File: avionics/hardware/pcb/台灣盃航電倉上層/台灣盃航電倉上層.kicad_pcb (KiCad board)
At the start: 4 copper layers, 80 x 80 mm, 38 parts, among them J1 SMA, J2 SMA, U1 LIS3MDL, U2 NEO-M9N, U3 E22-900T22S, U4 Connector

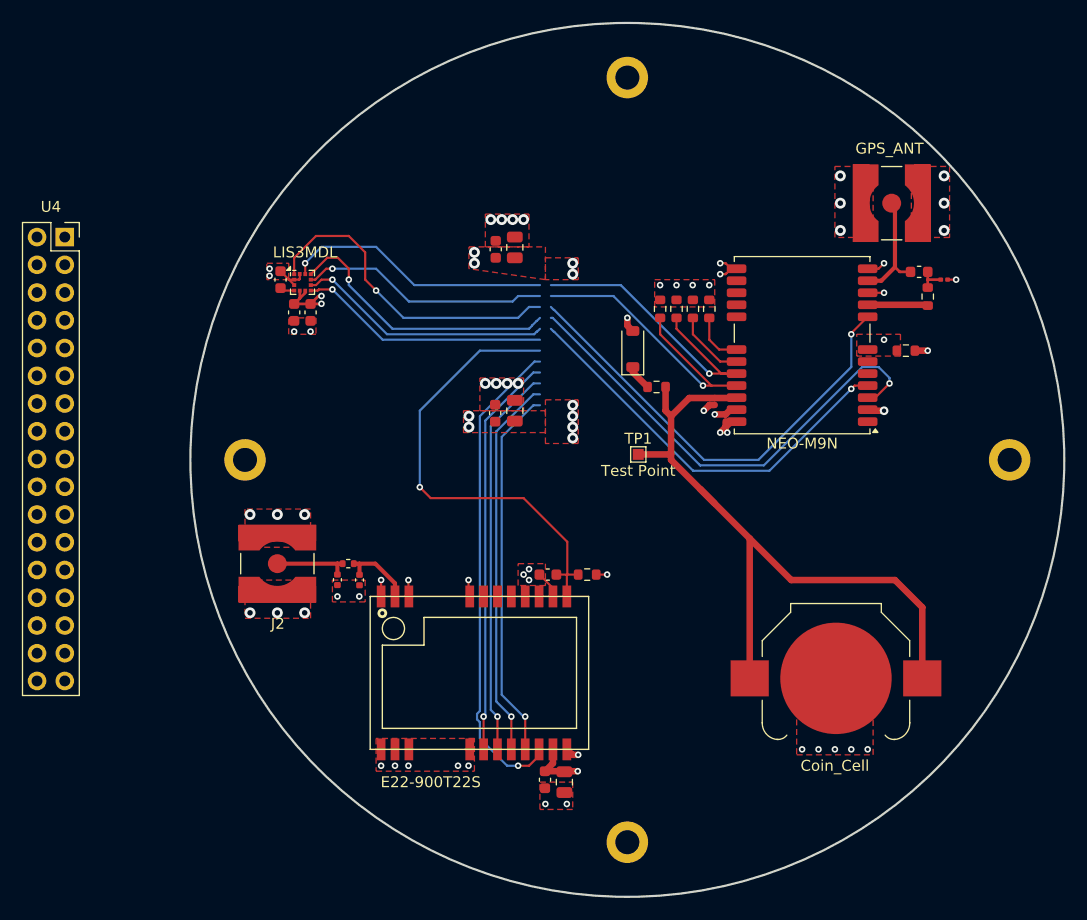
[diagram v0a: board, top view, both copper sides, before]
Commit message: 對上層PCB的布局進行了一些修改
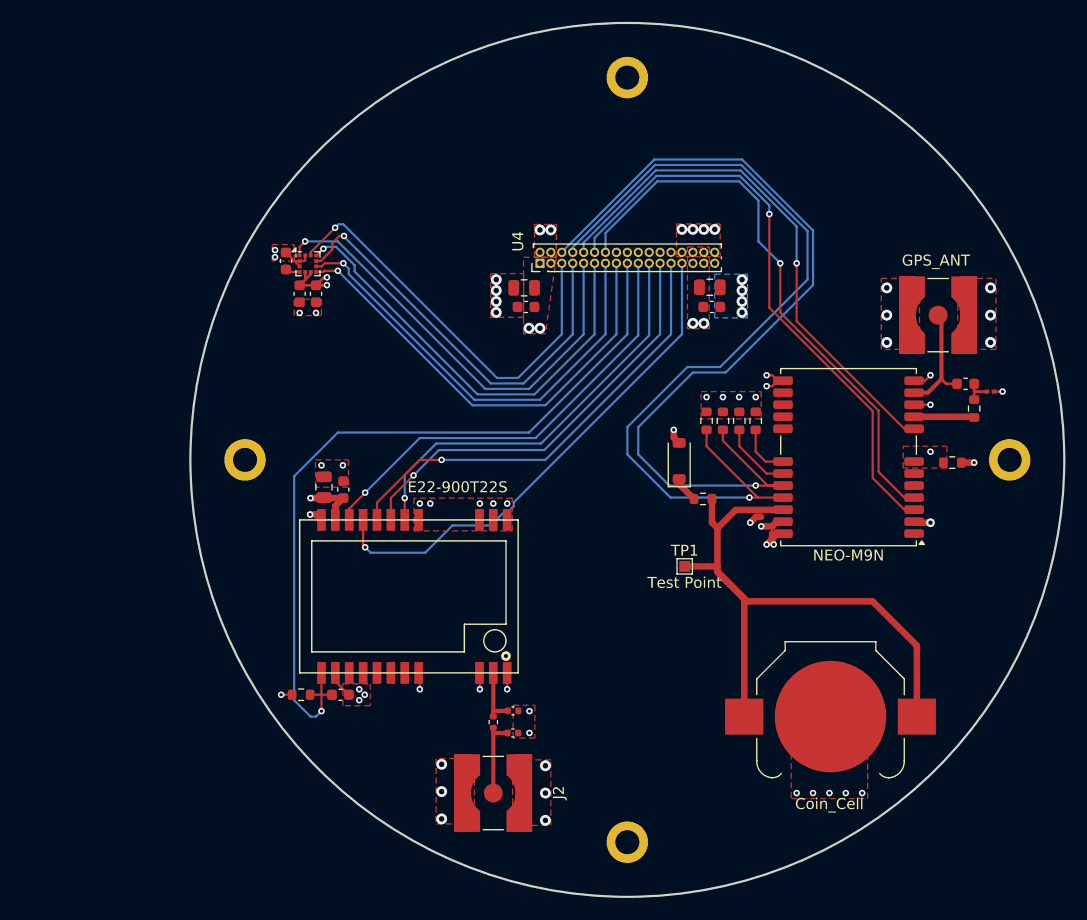
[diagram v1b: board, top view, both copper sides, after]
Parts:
- U4: footprint Connector_PinSocket_2.54mm:PinSocket_2x17_P2.54mm_Vertical -> Connector_PinHeader_1.00mm:PinHeader_2x17_P1.00mm_Vertical
- moved U4 43.6 mm to (139.0, 78.0), turned to 90 degrees
- moved C14 34.8 mm to (119.2, 98.5), turned to 90 degrees
- moved C15 32.3 mm to (121.0, 98.7), turned to 90 degrees
- moved J2 28.8 mm to (134.7, 126.5), turned to 90 degrees
- moved R9 28.4 mm to (117.1, 117.5), turned to 0 degrees
- moved C11 22.1 mm to (154.7, 82.0), turned to 0 degrees
- moved C12 21.9 mm to (120.7, 117.5), turned to 0 degrees
- moved C9 21.3 mm to (136.5, 121.0), turned to 0 degrees
- moved C8 21.1 mm to (154.6, 80.2), turned to 0 degrees
- moved R8 19.7 mm to (134.7, 120.0), turned to 90 degrees
- moved C13 18.5 mm to (136.5, 119.0), turned to 0 degrees
- moved C1 11.1 mm to (160.2, 102.4)
- moved C5 11.1 mm to (180.2, 89.8)
- moved C6 11.1 mm to (159.2, 100.9)
- moved D1 11.1 mm to (151.8, 96.1)
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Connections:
- U4 pad 31: +3V3 -> unconnected-(U4-5V-Pad31)
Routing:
- net GPS_TX: track 28.1 -> 80.4 mm
- net GPS_RX: track 29.1 -> 81.2 mm
- net LORA_RESET: track 42.9 -> 71.7 mm
- net INT_MAG: track 23.0 -> 41.8 mm
- net DRDY_MAG: track 23.5 -> 41.1 mm
- net SPI2_MISO: track 22.8 -> 38.8 mm
- net CS_MAG: track 25.6 -> 40.5 mm
- net INT_GPS: track 37.6 -> 52.1 mm
- net SPI2_MOSI: track 24.6 -> 38.3 mm
- net LORA_TX: track 35.0 -> 46.8 mm
- net GPS_PPS: track 43.9 -> 55.4 mm
- net SPI2_SCK: track 29.8 -> 41.2 mm
- net +BACKUP: track 66.3 -> 58.4 mm
- net GPS_RESET: track 42.0 -> 48.8 mm
- net LORA_RX: track 36.0 -> 41.4 mm
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- added copper zone on B.Cu, net GND

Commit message: 完成上層PCB
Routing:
- removed copper zone on B.Cu, net GND
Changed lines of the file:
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@@
+	)
+	(zone
+		(net 3)
+		(net_name "GND")
+		(layer "F.Cu")
+		(hatch edge 0.5)
+		(priority 9)
+		(connect_pads yes
+			(clearance 0.5)
+		)
+		(min_thickness 0.25)
+		(filled_areas_thickness no)
+		(fill yes
+			(thermal_gap 0.5)
+			(thermal_bridge_width 0.5)
+		)
+		(polygon
+			(pts
+				(xy 155 79) (xy 158 79) (xy 158 83) (xy 155 83)
+			)
+		)
 	)
 	(zone
@@
 			)
 		)
-	)
-	(zone
-		(net 3)
-		(net_name "GND")
-		(layer "B.Cu")
-		(hatch edge 0.5)
-		(priority 9)
-		(connect_pads yes
-			(clearance 0.5)
-		)
-		(min_thickness 0.25)
-		(filled_areas_thickness no)
-		(fill yes
-			(thermal_gap 0.5)
-			(thermal_bridge_width 0.5)
-		)
-		(polygon
-			(pts
-				(xy 155 79) (xy 158 79) (xy 158 83) (xy 155 83)
-			)
-		)

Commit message: 完成所有航電板設計
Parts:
- added G***: LOGO, Lumina et Umbrae:ISP_Logo, F.Cu at (128.0, 80.3)
- renumbered J2 to LORA_ANT
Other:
- board text added: "Layer 2 v2026.4"
